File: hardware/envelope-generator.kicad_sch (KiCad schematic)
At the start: 102 parts, among them J1 Power bus, J10 CV 2 In, J2 Dual or Voice 1 Out, J3 Conn_01x03_Socket, J4 EG 2 Out, J5 Gate 1 In, J6 CAN, J7 Gate 2 In, J8 SWD, J9 CV 1 In, SW1 RESET_SW, SW3 USER_SW, U1 TL072, U10 CD4051B, U2 MC34063AD, U3 MCP6004, U4 LM4040DBZ-3.0, U5 STM32G0B1CET6, U6 PEL12D-4225S-S2024, U7 LM4040DBZ-3.0, U8 LM393, U9 TCAN3413, Y1 16MHz

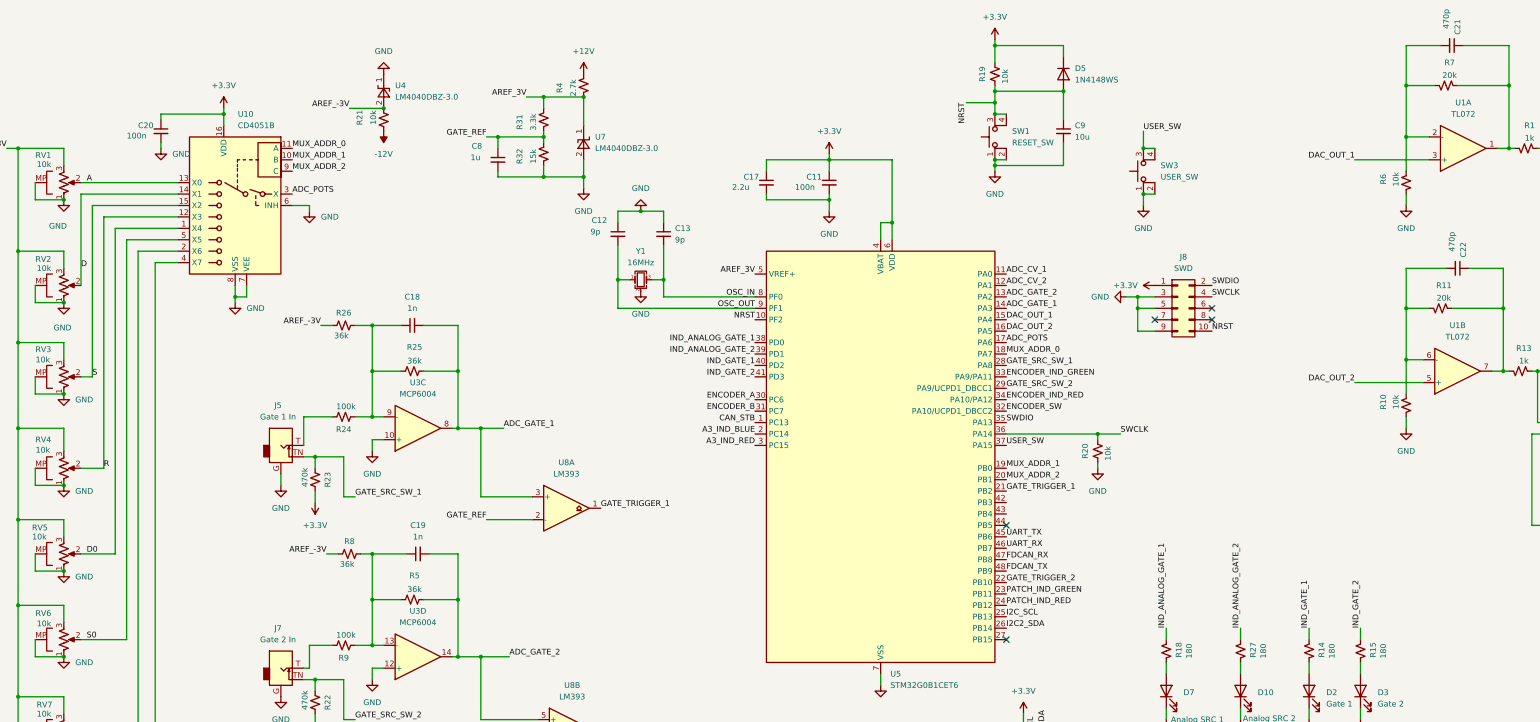
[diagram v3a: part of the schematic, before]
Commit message: Issue #4 - Add capability for negative output (#22)
* Modify the circuit to enable negative output

* Modify engines to support positive and negative output

* Improve the way to write value to DAC
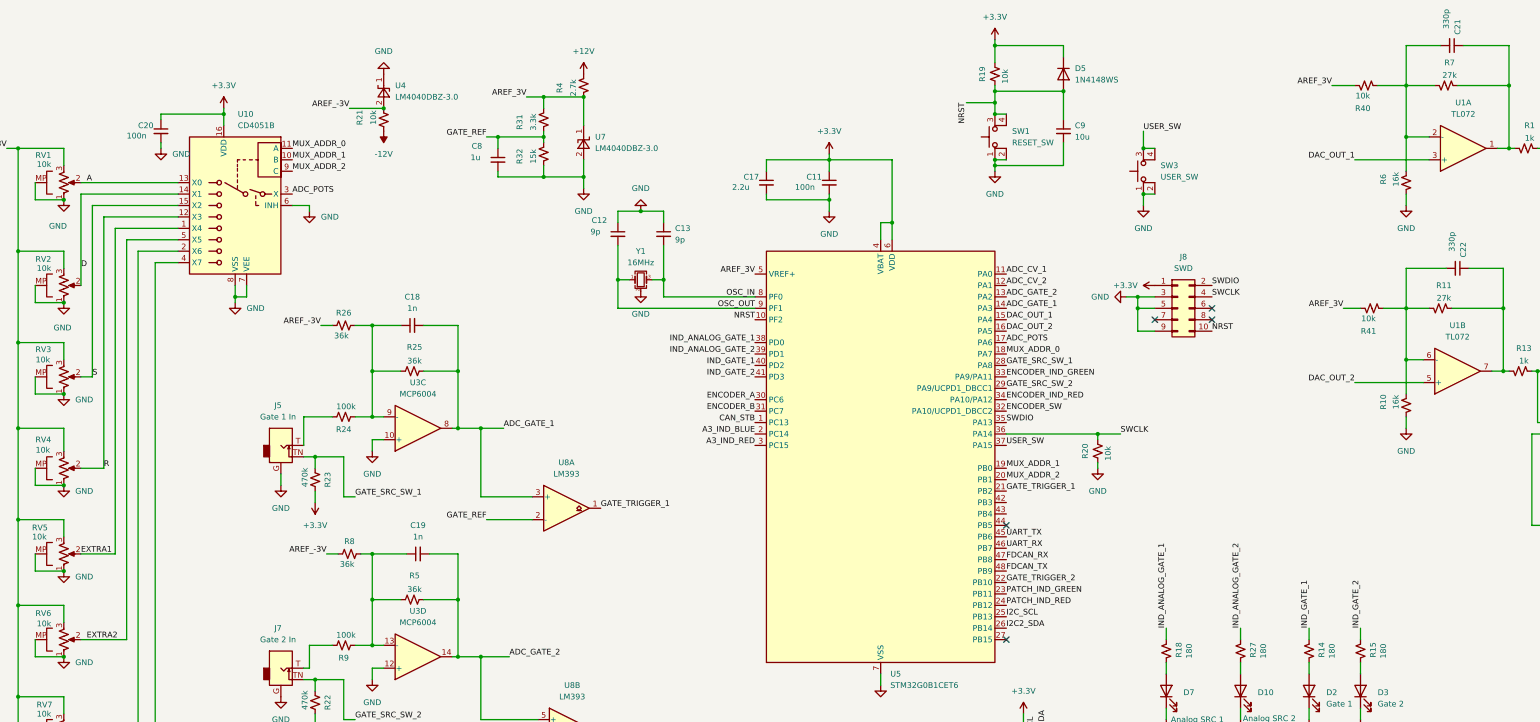
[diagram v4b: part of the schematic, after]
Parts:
- added R40, R41: 10k, Resistor_SMD:R_0603_1608Metric, symbol Device:R_Small_US
- C21, C22: value 470p -> 330p
- R10, R6: value 10k -> 16k
- R11, R7: value 20k -> 27k
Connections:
- net AREF_3V: now also R40.1, R41.1
- net at C22.2, R10.1, R11.2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: now also R41.2
- net at C21.2, R6.1, R7.2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: now also R40.2
- net D0 renamed EXTRA1
- net S0 renamed EXTRA2
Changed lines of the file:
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@@
 	(wire
 		(pts
+			(xy 331.47 81.28) (xy 336.55 81.28)
+		)
+		(stroke
+			(width 0)
+			(type default)
+		)
+	)
+	(wire
+		(pts
 			(xy 369.57 57.15) (xy 370.84 57.15)
 		)
@@
 	(wire
 		(pts
+			(xy 41.91 154.94) (xy 52.07 154.94)
+		)
+		(stroke
+			(width 0)
+			(type default)
+		)
+	)
+	(wire
+		(pts
 			(xy 154.94 256.54) (xy 167.64 256.54)
 		)
@@
 	(wire
 		(pts
+			(xy 330.2 31.75) (xy 336.55 31.75)
+		)
+		(stroke
+			(width 0)
+			(type default)
+		)
+	)
+	(wire
+		(pts
 			(xy 106.68 135.89) (xy 114.3 135.89)
 		)
@@
 	(wire
 		(pts
-			(xy 203.2 247.65) (xy 203.2 240.03)
+			(xy 320.04 31.75) (xy 325.12 31.75)
 		)
 		(stroke
@@
 	(wire
 		(pts
-			(xy 106.68 113.03) (xy 106.68 110.49)
+			(xy 203.2 247.65) (xy 203.2 240.03)
 		)
 		(stroke
@@
 	(wire
 		(pts
-			(xy 242.57 261.62) (xy 242.57 250.19)
+			(xy 106.68 113.03) (xy 106.68 110.49)
 		)
 		(stroke
@@
 	(wire
 		(pts
-			(xy 52.07 154.94) (xy 41.91 154.94)
+			(xy 242.57 261.62) (xy 242.57 250.19)
 		)
 		(stroke
@@
 	(wire
 		(pts
+			(xy 322.58 81.28) (xy 326.39 81.28)
+		)
+		(stroke
+			(width 0)
+			(type default)
+		)
+	)
+	(wire
+		(pts
 			(xy 299.72 152.4) (xy 299.72 154.94)
 		)
@@
 		)
 	)
-	(label "D0"
-		(at 43.18 135.89 0)
+	(label "EXTRA1"
+		(at 41.91 135.89 0)
 		(effects
 			(font
@@
 		)
 	)
-	(label "S0"
+	(label "EXTRA2"
 		(at 43.18 154.94 0)
 		(effects
@@
 		)
 	)
+	(label "AREF_3V"
+		(at 320.04 31.75 180)
+		(effects
+			(font
+				(size 1.27 1.27)
+			)
+			(justify right bottom)
+		)
+	)
 	(label "GATE_SRC_SW_1"
 		(at 102.87 123.19 0)
@@
 		)
 	)
+	(label "AREF_3V"
+		(at 322.58 81.28 180)
+		(effects
+			(font
+				(size 1.27 1.27)
+			)
+			(justify right bottom)
+		)
+	)
 	(label "PATCH_IND_GREEN"
 		(at 247.65 144.78 0)
@@
 	)
 	(symbol
+		(lib_id "Device:R_Small_US")
+		(at 328.93 81.28 90)
+		(mirror x)
+		(unit 1)
+		(exclude_from_sim no)
+		(in_bom yes)
+		(on_board yes)
+		(dnp no)
+		(property "Reference" "R41"
+			(at 328.168 86.36 90)
+			(effects
+				(font
+					(size 1.27 1.27)
+				)
+			)
+		)
+		(property "Value" "10k"
+			(at 328.168 83.566 90)
+			(effects
+				(font
+					(size 1.27 1.27)
+				)
+			)
+		)
+		(property "Footprint" "Resistor_SMD:R_0603_1608Metric"
+			(at 328.93 81.28 0)
+			(effects
+				(font
+					(size 1.27 1.27)
+				)
+				(hide yes)
+			)
+		)
+		(property "Datasheet" "~"
+			(at 328.93 81.28 0)
+			(effects
+				(font
+					(size 1.27 1.27)
+				)
+				(hide yes)
+			)
+		)
+		(property "Description" "Resistor, small US symbol"
+			(at 328.93 81.28 0)
+			(effects
+				(font
+					(size 1.27 1.27)
+				)
+				(hide yes)
+			)
+		)
+		(pin "1"
+		)
+		(pin "2"
+		)
+		(instances
+			(project "envelope-generator"
+				(path "/ae80d454-00d5-4ccf-83a7-5fd8c4202bfc"
+					(reference "R41")
+					(unit 1)
+				)
+			)
+		)
+	)
+	(symbol
 		(lib_id "Regulator_Switching:MC34063AD")
 		(at 167.64 240.03 0)
@@
 			)
 		)
-		(property "Value" "470p"
+		(property "Value" "330p"
 			(at 346.71 64.262 0)
 			(effects
@@
 	(symbol
 		(lib_id "Device:R_Small_US")
+		(at 327.66 31.75 90)
+		(mirror x)
+		(unit 1)
+		(exclude_from_sim no)
+		(in_bom yes)
+		(on_board yes)
+		(dnp no)
+		(property "Reference" "R40"
+			(at 326.898 36.83 90)
+			(effects
+				(font
+					(size 1.27 1.27)
+				)
+			)
+		)
+		(property "Value" "10k"
+			(at 326.898 34.036 90)
+			(effects
+				(font
+					(size 1.27 1.27)
+				)
+			)
+		)
+		(property "Footprint" "Resistor_SMD:R_0603_1608Metric"
+			(at 327.66 31.75 0)
+			(effects
+				(font
+					(size 1.27 1.27)
+				)
+				(hide yes)
+			)
+		)
+		(property "Datasheet" "~"
+			(at 327.66 31.75 0)
+			(effects
+				(font
+					(size 1.27 1.27)
+				)
+				(hide yes)
+			)
+		)
+		(property "Description" "Resistor, small US symbol"
+			(at 327.66 31.75 0)
+			(effects
+				(font
+					(size 1.27 1.27)
+				)
+				(hide yes)
+			)
+		)
+		(pin "1"
+		)
+		(pin "2"
+		)
+		(instances
+			(project "envelope-generator"
+				(path "/ae80d454-00d5-4ccf-83a7-5fd8c4202bfc"
+					(reference "R40")
+					(unit 1)
+				)
+			)
+		)
+	)
+	(symbol
+		(lib_id "Device:R_Small_US")
 		(at 83.82 195.58 90)
 		(unit 1)
@@
 			)
 		)
-		(property "Value" "20k"
+		(property "Value" "27k"
 			(at 344.932 78.994 90)
 			(effects
@@
 			)
 		)
-		(property "Value" "10k"
+		(property "Value" "16k"
 			(at 334.264 52.578 90)
 			(effects
@@
 			)
 		)
-		(property "Value" "10k"
+		(property "Value" "16k"
 			(at 334.264 102.108 90)
 			(effects
@@
 			)
 		)
-		(property "Value" "20k"
+		(property "Value" "27k"
 			(at 346.202 29.464 90)
 			(effects
@@
 			)
 		)
-		(property "Value" "470p"
+		(property "Value" "330p"
 			(at 345.44 14.732 0)
 			(effects

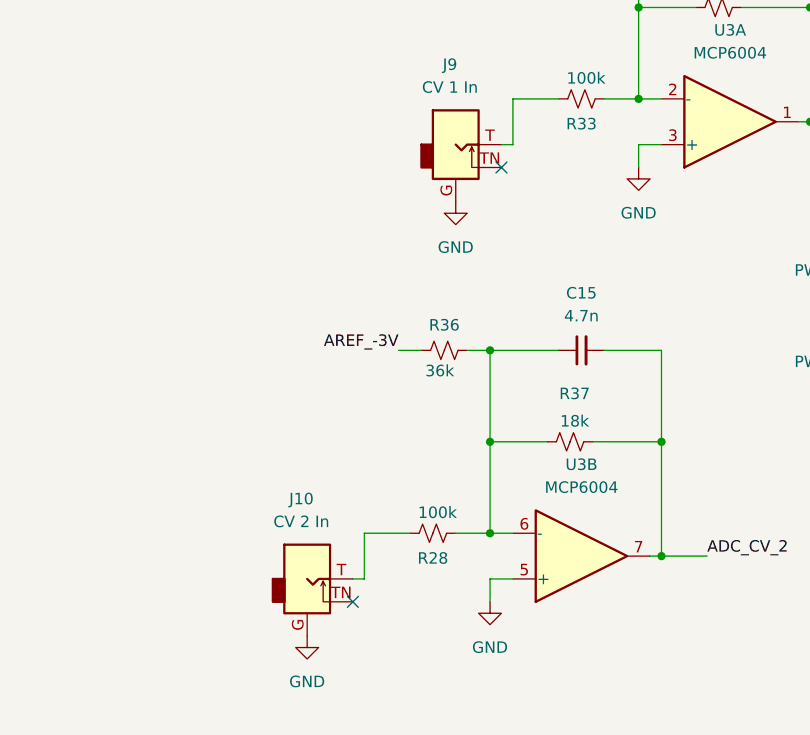
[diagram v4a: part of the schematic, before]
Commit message: Fix circuit and PCB issues
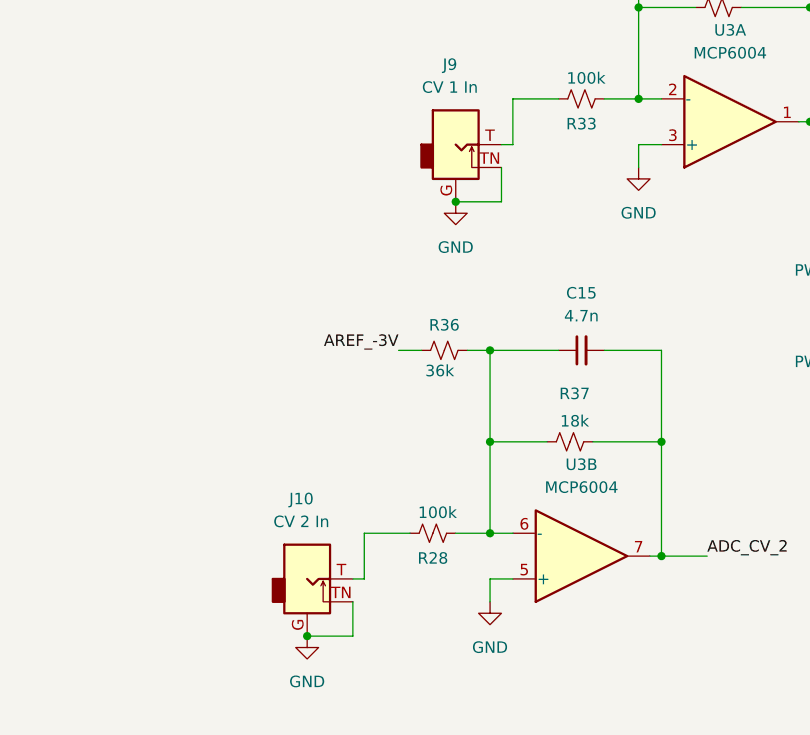
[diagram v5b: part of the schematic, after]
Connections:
- net GND: now also J10.TN, J9.TN
- no-connect marks 7 -> 5
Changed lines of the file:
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@@
 	)
 	(junction
+		(at 52.07 275.59)
+		(diameter 0)
+		(color 0 0 0 0)
+	)
+	(junction
 		(at 135.89 242.57)
 		(diameter 0)
@@
 	)
 	(junction
+		(at 68.58 227.33)
+		(diameter 0)
+		(color 0 0 0 0)
+	)
+	(junction
 		(at 27.94 147.32)
 		(diameter 0)
@@
 	)
 	(no_connect
-		(at 73.66 223.52)
-	)
-	(no_connect
-		(at 57.15 271.78)
-	)
-	(no_connect
 		(at 293.37 81.28)
 	)
@@
 	(wire
 		(pts
+			(xy 73.66 223.52) (xy 73.66 227.33)
+		)
+		(stroke
+			(width 0)
+			(type default)
+		)
+	)
+	(wire
+		(pts
 			(xy 161.29 59.69) (xy 166.37 59.69)
 		)
@@
 	(wire
 		(pts
+			(xy 57.15 271.78) (xy 57.15 275.59)
+		)
+		(stroke
+			(width 0)
+			(type default)
+		)
+	)
+	(wire
+		(pts
 			(xy 335.28 180.34) (xy 340.36 180.34)
 		)
@@
 	(wire
 		(pts
+			(xy 57.15 275.59) (xy 52.07 275.59)
+		)
+		(stroke
+			(width 0)
+			(type default)
+		)
+	)
+	(wire
+		(pts
 			(xy 242.57 273.05) (xy 242.57 266.7)
 		)
@@
 		)
 		(stroke
+			(width 0)
+			(type default)
+		)
+	)
+	(wire
+		(pts
+			(xy 73.66 227.33) (xy 68.58 227.33)
+		)
+		(stroke
